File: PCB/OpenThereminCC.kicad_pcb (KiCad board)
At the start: 2 copper layers, 60 x 100 mm, 109 parts, among them P1 10k, P2 10k, P3 10k, P4 10k, P5 SP+, P6 SP-, P7 CONN_01X01, P8 CONN_01X01, P9 CONN_01X01, SW1 SW_PUSH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

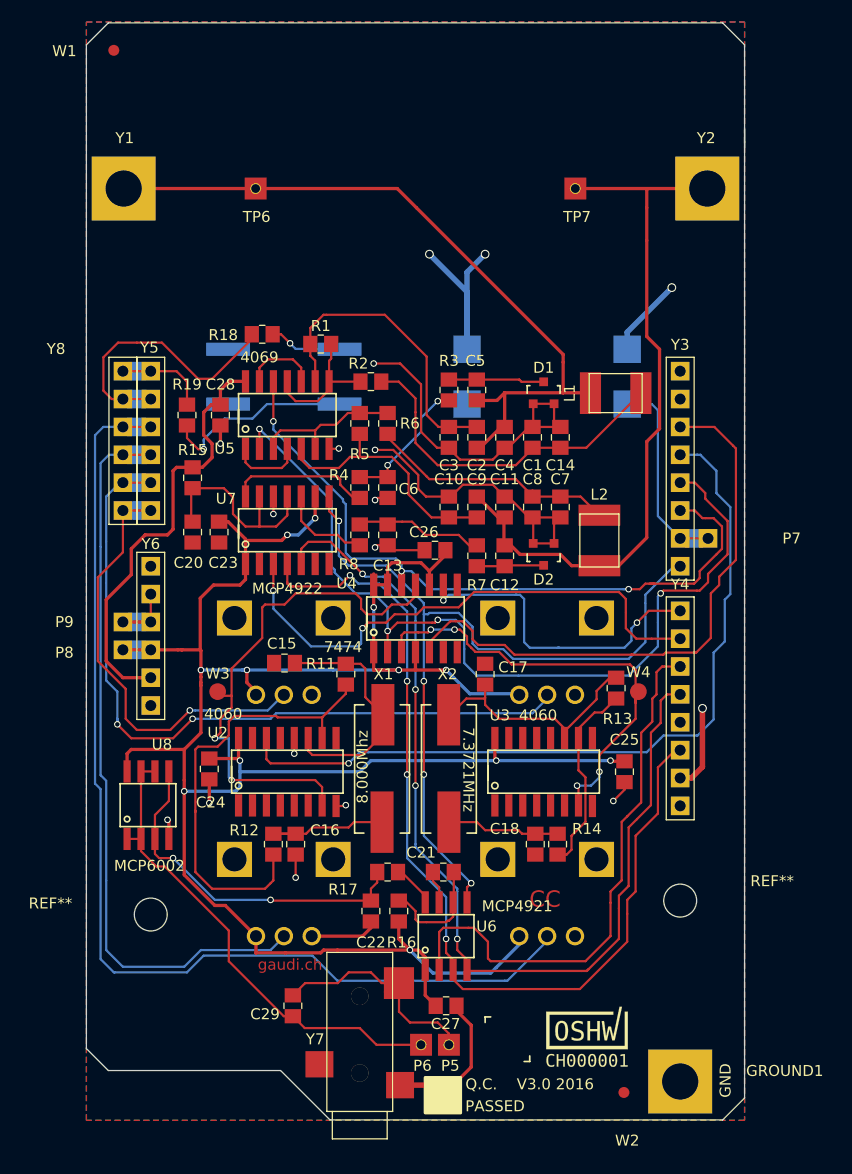
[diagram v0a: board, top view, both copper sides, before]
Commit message: Increased and spaced vias. Had to manually add thermal reliefs as they were ignored in gerber generation
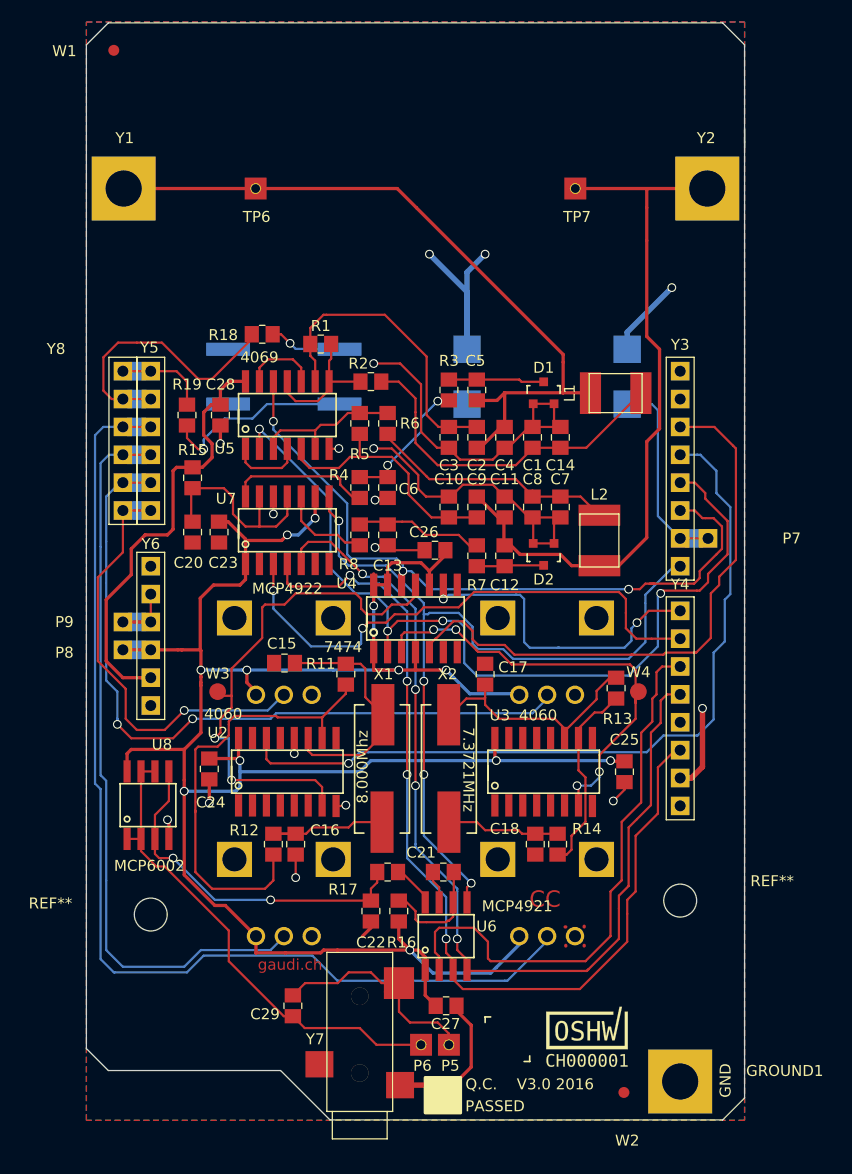
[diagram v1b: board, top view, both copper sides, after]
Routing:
- net GND: track 142.8 -> 138.6 mm
- net F_VOL: track 54.0 -> 54.8 mm
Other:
- net class Default: via_dia 0.6 -> 0.8; via_drill 0.4 -> 0.6
- net class Power: via_dia 0.6 -> 0.8; via_drill 0.4 -> 0.6
- rule via_min_drill: 0.3 -> 0.6
- rule via_min_size: 0.4 -> 0.8
